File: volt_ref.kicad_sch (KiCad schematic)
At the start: 11 parts, among them U11 ADR1001AEZ

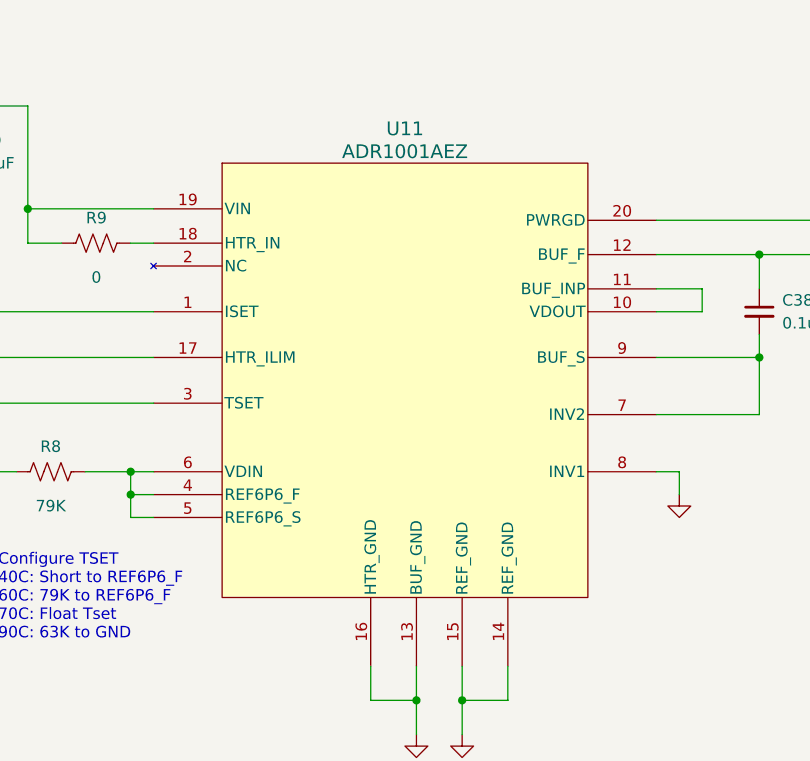
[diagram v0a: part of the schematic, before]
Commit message: Add ADC monitor circuit
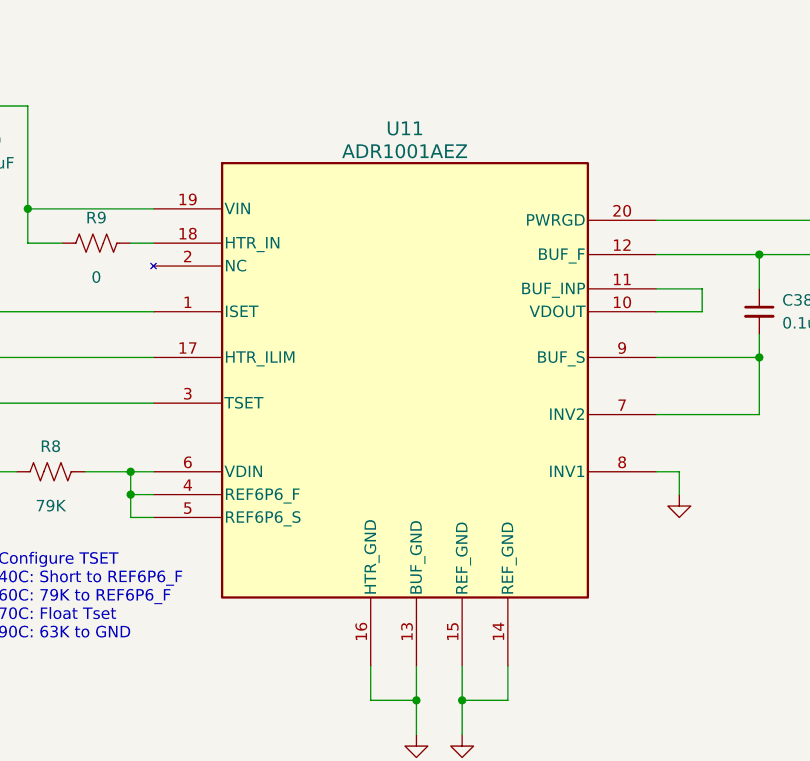
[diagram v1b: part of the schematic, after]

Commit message: Add DCCT ADCs
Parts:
- renumbered C39 to C48, C40 to C49, C38 to C50, C42 to C51, C41 to C52, R7 to R11, R6 to R12, R5 to R13, R8 to R14, R9 to R15, U11 to U12
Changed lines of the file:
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@@
 		(on_board yes)
 		(dnp no)
-		(property "Reference" "C41"
+		(property "Reference" "C52"
 			(at 275.59 105.4162 0)
 			(effects
@@
 			(project "psc_daughter_brd"
 				(path "/40891cc8-bf64-41f4-8f69-a607d7b280eb/dea95122-986e-41c8-b99e-e429cc6f4cd5/4999e499-3966-4a05-8928-c40234f9b048"
-					(reference "C41")
+					(reference "C52")
 					(unit 1)
 				)
@@
 		(on_board yes)
 		(dnp no)
-		(property "Reference" "C38"
+		(property "Reference" "C50"
 			(at 250.19 106.6862 0)
 			(effects
@@
 			(project "psc_daughter_brd"
 				(path "/40891cc8-bf64-41f4-8f69-a607d7b280eb/dea95122-986e-41c8-b99e-e429cc6f4cd5/4999e499-3966-4a05-8928-c40234f9b048"
-					(reference "C38")
+					(reference "C50")
 					(unit 1)
 				)
@@
 		(dnp no)
 		(fields_autoplaced yes)
-		(property "Reference" "#PWR072"
+		(property "Reference" "#PWR081"
 			(at 157.48 101.6 0)
 			(effects
@@
 			(project "psc_daughter_brd"
 				(path "/40891cc8-bf64-41f4-8f69-a607d7b280eb/dea95122-986e-41c8-b99e-e429cc6f4cd5/4999e499-3966-4a05-8928-c40234f9b048"
-					(reference "#PWR072")
+					(reference "#PWR081")
 					(unit 1)
 				)
@@
 		(on_board yes)
 		(dnp no)
-		(property "Reference" "R6"
+		(property "Reference" "R12"
 			(at 145.542 128.27 0)
 			(effects
@@
 			(project "psc_daughter_brd"
 				(path "/40891cc8-bf64-41f4-8f69-a607d7b280eb/dea95122-986e-41c8-b99e-e429cc6f4cd5/4999e499-3966-4a05-8928-c40234f9b048"
-					(reference "R6")
+					(reference "R12")
 					(unit 1)
 				)
@@
 		(dnp no)
 		(fields_autoplaced yes)
-		(property "Reference" "#PWR063"
+		(property "Reference" "#PWR077"
 			(at 140.97 143.51 0)
 			(effects
@@
 			(project ""
 				(path "/40891cc8-bf64-41f4-8f69-a607d7b280eb/dea95122-986e-41c8-b99e-e429cc6f4cd5/4999e499-3966-4a05-8928-c40234f9b048"
-					(reference "#PWR063")
+					(reference "#PWR077")
 					(unit 1)
 				)
@@
 		(dnp no)
 		(fields_autoplaced yes)
-		(property "Reference" "#PWR073"
+		(property "Reference" "#PWR086"
 			(at 261.62 118.11 0)
 			(effects
@@
 			(project "psc_daughter_brd"
 				(path "/40891cc8-bf64-41f4-8f69-a607d7b280eb/dea95122-986e-41c8-b99e-e429cc6f4cd5/4999e499-3966-4a05-8928-c40234f9b048"
-					(reference "#PWR073")
+					(reference "#PWR086")
 					(unit 1)
 				)
@@
 		(dnp no)
 		(fields_autoplaced yes)
-		(property "Reference" "#PWR071"
+		(property "Reference" "#PWR079"
 			(at 146.05 101.6 0)
 			(effects
@@
 			(project "psc_daughter_brd"
 				(path "/40891cc8-bf64-41f4-8f69-a607d7b280eb/dea95122-986e-41c8-b99e-e429cc6f4cd5/4999e499-3966-4a05-8928-c40234f9b048"
-					(reference "#PWR071")
+					(reference "#PWR079")
 					(unit 1)
 				)
@@
 		(dnp no)
 		(fields_autoplaced yes)
-		(property "Reference" "U11"
+		(property "Reference" "U12"
 			(at 208.28 87.63 0)
 			(effects
@@
 			(project ""
 				(path "/40891cc8-bf64-41f4-8f69-a607d7b280eb/dea95122-986e-41c8-b99e-e429cc6f4cd5/4999e499-3966-4a05-8928-c40234f9b048"
-					(reference "U11")
+					(reference "U12")
 					(unit 1)
 				)
@@
 		(dnp no)
 		(fields_autoplaced yes)
-		(property "Reference" "#PWR069"
+		(property "Reference" "#PWR087"
 			(at 273.05 118.11 0)
 			(effects
@@
 			(project "psc_daughter_brd"
 				(path "/40891cc8-bf64-41f4-8f69-a607d7b280eb/dea95122-986e-41c8-b99e-e429cc6f4cd5/4999e499-3966-4a05-8928-c40234f9b048"
-					(reference "#PWR069")
+					(reference "#PWR087")
 					(unit 1)
 				)
@@
 		(dnp no)
 		(fields_autoplaced yes)
-		(property "Reference" "#PWR068"
+		(property "Reference" "#PWR085"
 			(at 238.76 134.62 0)
 			(effects
@@
 			(project "psc_daughter_brd"
 				(path "/40891cc8-bf64-41f4-8f69-a607d7b280eb/dea95122-986e-41c8-b99e-e429cc6f4cd5/4999e499-3966-4a05-8928-c40234f9b048"
-					(reference "#PWR068")
+					(reference "#PWR085")
 					(unit 1)
 				)
@@
 		(dnp no)
 		(fields_autoplaced yes)
-		(property "Reference" "#PWR066"
+		(property "Reference" "#PWR084"
 			(at 214.63 161.29 0)
 			(effects
@@
 			(project "psc_daughter_brd"
 				(path "/40891cc8-bf64-41f4-8f69-a607d7b280eb/dea95122-986e-41c8-b99e-e429cc6f4cd5/4999e499-3966-4a05-8928-c40234f9b048"
-					(reference "#PWR066")
+					(reference "#PWR084")
 					(unit 1)
 				)
@@
 		(dnp no)
 		(fields_autoplaced yes)
-		(property "Reference" "#PWR067"
+		(property "Reference" "#PWR083"
 			(at 209.55 161.29 0)
 			(effects
@@
 			(project "psc_daughter_brd"
 				(path "/40891cc8-bf64-41f4-8f69-a607d7b280eb/dea95122-986e-41c8-b99e-e429cc6f4cd5/4999e499-3966-4a05-8928-c40234f9b048"
-					(reference "#PWR067")
+					(reference "#PWR083")
 					(unit 1)
 				)
@@
 		(dnp no)
 		(fields_autoplaced yes)
-		(property "Reference" "#PWR070"
+		(property "Reference" "#PWR078"
 			(at 146.05 77.47 0)
 			(effects
@@
 			(project "psc_daughter_brd"
 				(path "/40891cc8-bf64-41f4-8f69-a607d7b280eb/dea95122-986e-41c8-b99e-e429cc6f4cd5/4999e499-3966-4a05-8928-c40234f9b048"
-					(reference "#PWR070")
+					(reference "#PWR078")
 					(unit 1)
 				)
@@
 		(dnp no)
 		(fields_autoplaced yes)
-		(property "Reference" "#PWR065"
+		(property "Reference" "#PWR082"
 			(at 158.75 143.51 0)
 			(effects
@@
 			(project "psc_daughter_brd"
 				(path "/40891cc8-bf64-41f4-8f69-a607d7b280eb/dea95122-986e-41c8-b99e-e429cc6f4cd5/4999e499-3966-4a05-8928-c40234f9b048"
-					(reference "#PWR065")
+					(reference "#PWR082")
 					(unit 1)
 				)
@@
 		(on_board yes)
 		(dnp no)
-		(property "Reference" "R7"
+		(property "Reference" "R11"
 			(at 136.906 127.508 0)
 			(effects
@@
 			(project "psc_daughter_brd"
 				(path "/40891cc8-bf64-41f4-8f69-a607d7b280eb/dea95122-986e-41c8-b99e-e429cc6f4cd5/4999e499-3966-4a05-8928-c40234f9b048"
-					(reference "R7")
+					(reference "R11")
 					(unit 1)
 				)
@@
 		(on_board yes)
 		(dnp no)
-		(property "Reference" "R8"
+		(property "Reference" "R14"
 			(at 168.91 122.936 90)
 			(effects
@@
 			(project "psc_daughter_brd"
 				(path "/40891cc8-bf64-41f4-8f69-a607d7b280eb/dea95122-986e-41c8-b99e-e429cc6f4cd5/4999e499-3966-4a05-8928-c40234f9b048"
-					(reference "R8")
+					(reference "R14")
 					(unit 1)
 				)
@@
 		(on_board yes)
 		(dnp no)
-		(property "Reference" "C42"
+		(property "Reference" "C51"
 			(at 264.16 105.4162 0)
 			(effects
@@
 			(project "psc_daughter_brd"
 				(path "/40891cc8-bf64-41f4-8f69-a607d7b280eb/dea95122-986e-41c8-b99e-e429cc6f4cd5/4999e499-3966-4a05-8928-c40234f9b048"
-					(reference "C42")
+					(reference "C51")
 					(unit 1)
 				)
@@
 		(dnp no)
 		(fields_autoplaced yes)
-		(property "Reference" "#PWR064"
+		(property "Reference" "#PWR080"
 			(at 149.86 143.51 0)
 			(effects
@@
 			(project "psc_daughter_brd"
 				(path "/40891cc8-bf64-41f4-8f69-a607d7b280eb/dea95122-986e-41c8-b99e-e429cc6f4cd5/4999e499-3966-4a05-8928-c40234f9b048"
-					(reference "#PWR064")
+					(reference "#PWR080")
 					(unit 1)
 				)
@@
 		(on_board yes)
 		(dnp no)
-		(property "Reference" "R9"
+		(property "Reference" "R15"
 			(at 173.99 97.536 90)
 			(effects
@@
 			(project "psc_daughter_brd"
 				(path "/40891cc8-bf64-41f4-8f69-a607d7b280eb/dea95122-986e-41c8-b99e-e429cc6f4cd5/4999e499-3966-4a05-8928-c40234f9b048"
-					(reference "R9")
+					(reference "R15")
 					(unit 1)
 				)
@@
 		(on_board yes)
 		(dnp no)
-		(property "Reference" "C40"
+		(property "Reference" "C49"
 			(at 160.02 88.9062 0)
 			(effects
@@
 			(project "psc_daughter_brd"
 				(path "/40891cc8-bf64-41f4-8f69-a607d7b280eb/dea95122-986e-41c8-b99e-e429cc6f4cd5/4999e499-3966-4a05-8928-c40234f9b048"
-					(reference "C40")
+					(reference "C49")
 					(unit 1)
 				)
@@
 		(on_board yes)
 		(dnp no)
-		(property "Reference" "C39"
+		(property "Reference" "C48"
 			(at 148.59 88.9062 0)
 			(effects
@@
 			(project "psc_daughter_brd"
 				(path "/40891cc8-bf64-41f4-8f69-a607d7b280eb/dea95122-986e-41c8-b99e-e429cc6f4cd5/4999e499-3966-4a05-8928-c40234f9b048"
-					(reference "C39")
+					(reference "C48")
 					(unit 1)
 				)
@@
 		(on_board yes)
 		(dnp no)
-		(property "Reference" "R5"
+		(property "Reference" "R13"
 			(at 153.924 128.27 0)
 			(effects
@@
 			(project "psc_daughter_brd"
 				(path "/40891cc8-bf64-41f4-8f69-a607d7b280eb/dea95122-986e-41c8-b99e-e429cc6f4cd5/4999e499-3966-4a05-8928-c40234f9b048"
-					(reference "R5")
-					(unit 1)
-				)
+					(reference "R13")
+					(unit 1)
+				)

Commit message: Finish layout
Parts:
- added C32: 1uF, Capacitor_SMD:C_0603_1608Metric, symbol Device:C_Small
- C48, C52: MFG (none) -> Samsung; MFG_PN (none) -> CL10A106MA8NRNC
- C49, C50, C51: MFG (none) -> Taiyo Yuden; MFG_PN (none) -> TMK105BJ104KV-F
- R11: MFG (none) -> Panasonic; MFG_PN (none) -> ERJ-2RKF1200X
- R12: Cost (none) -> .01; MFG (none) -> Panasonic; MFG_PN (none) -> ERJ-2RKF10R0X
- R13: value DNP -> 63K; MFG (none) -> Panasonic; MFG_PN (none) -> ERJ-2RKF6342X; now not fitted
- R14: value 79K -> 78.7K; MFG (none) -> Panasonic; MFG_PN (none) -> ERJ-2RKF7872X
- R15: MFG (none) -> Panasonic; MFG_PN (none) -> ERJ-2GE0R00X
- U12: Cost (none) -> 100.10; MFG (none) -> Analog Devices; MFG_PN (none) -> ADR1001AEZ
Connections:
- net GND: now also C32.2
- net at U12.10 (VDOUT), U12.11 (BUF_INP): now also C32.1
- net PWR_GOOD: no longer names the net of U12.20 (PWRGD)
- no-connect marks 0 -> 1
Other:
- moved on the sheet: C50, C51, C52
